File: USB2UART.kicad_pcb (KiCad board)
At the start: 2 copper layers, 43.9 x 34.3 mm, 33 parts, among them J1 Conn_01x04, J2 Conn_01x03, J3 Conn_01x03, J4 Conn_01x04, J5 Conn_01x04, Q1 S8050, U1 CH340E, U2 CH340E, U3 HX9193, U6 SL2.1S, U7 CH340E, U8 CH340E, Y1 12M

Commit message: iterative optimization
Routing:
- net +5V: track 79.7 -> 78.8 mm

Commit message: iterative optimization
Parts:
- moved D8 1.58 mm to (89.7, 82.9)
- moved R13 1.58 mm to (93.4, 82.9)
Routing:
- net VCC: track 104.9 -> 103.1 mm

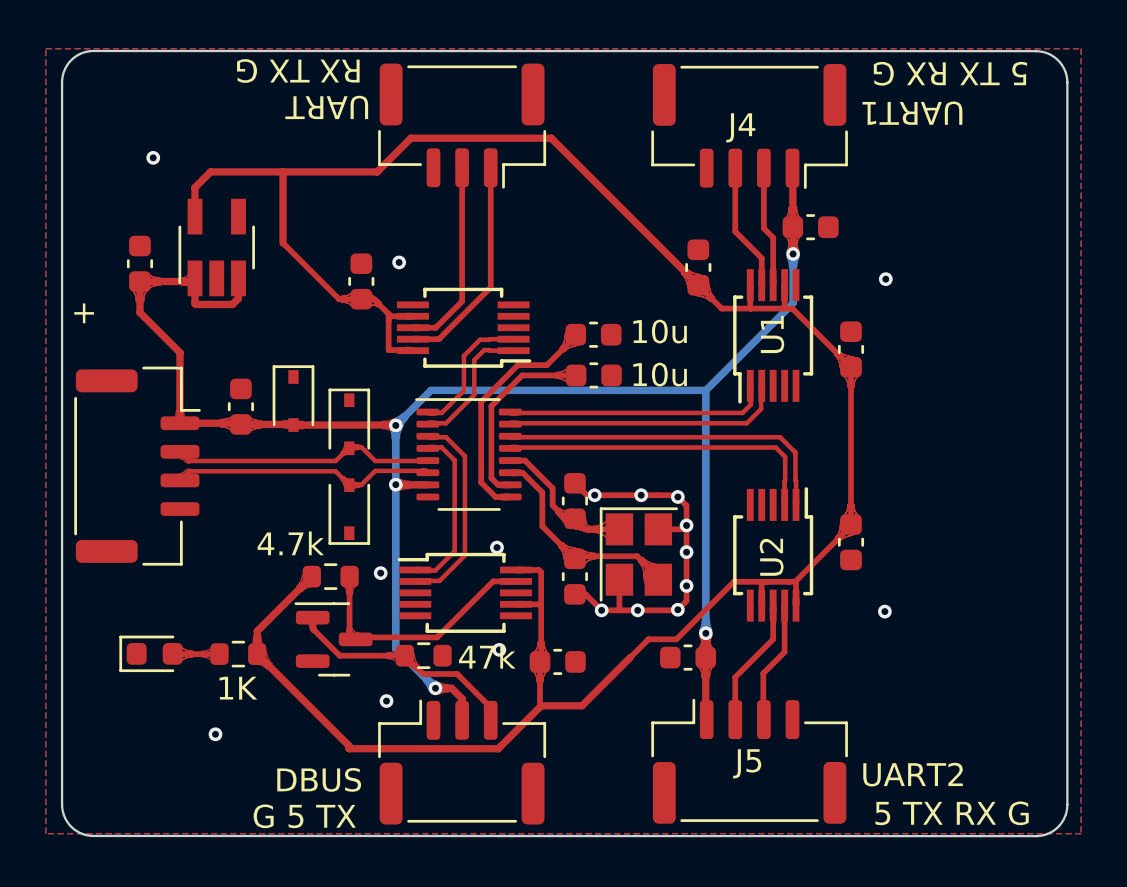
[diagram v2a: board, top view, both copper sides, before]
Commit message: Change some routings & add teardrops
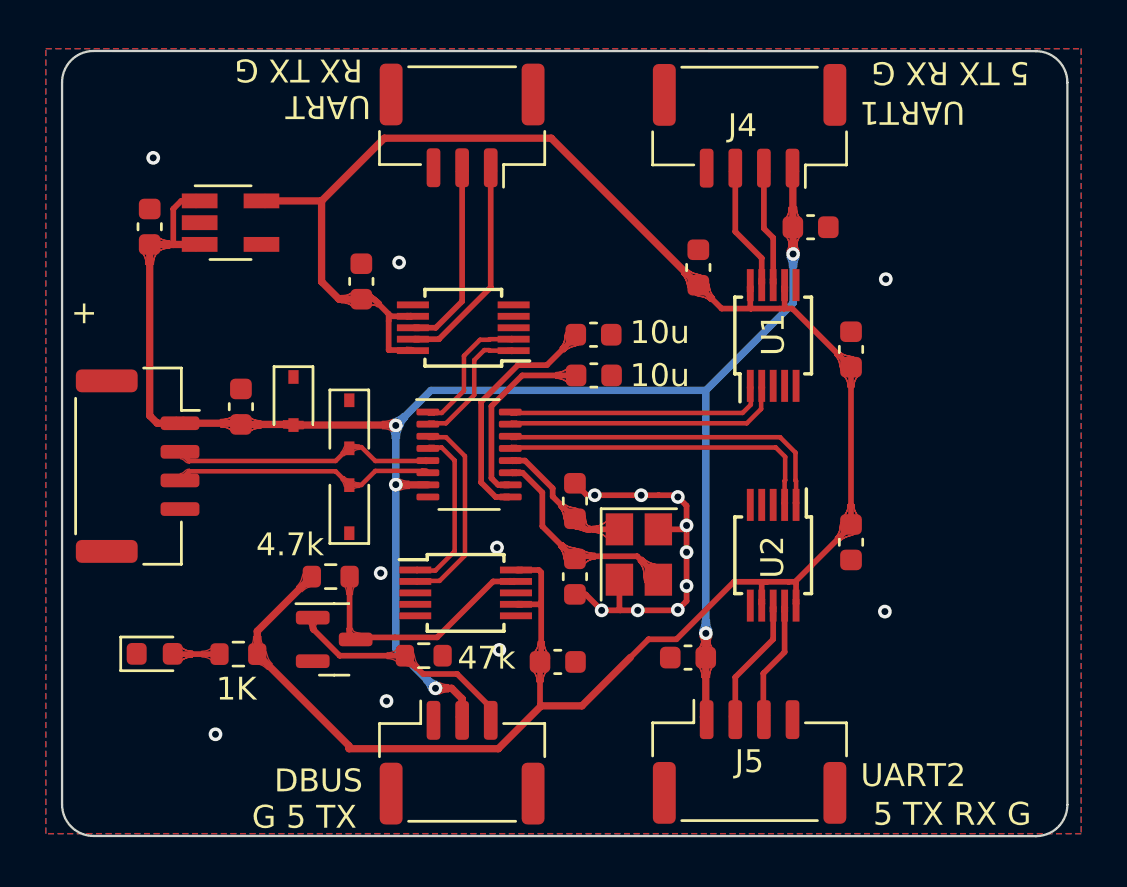
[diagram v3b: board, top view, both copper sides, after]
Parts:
- moved C26 1.67 mm to (89.5, 64.3)
- moved U3 1.24 mm to (93.0, 64.1), turned to 0 degrees
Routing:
- net VCC: track 103.1 -> 97.2 mm
- net +5V: track 78.8 -> 79.4 mm
